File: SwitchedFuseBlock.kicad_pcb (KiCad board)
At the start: 2 copper layers, 9 parts

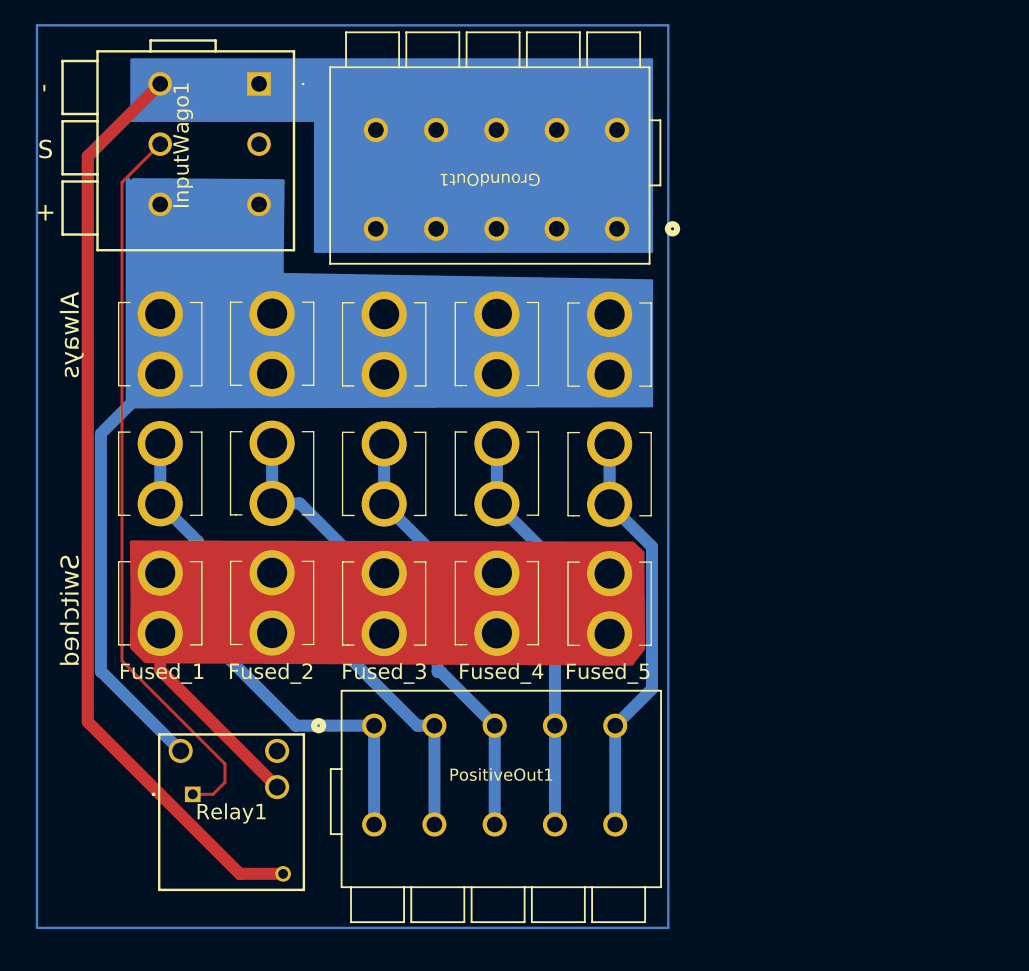
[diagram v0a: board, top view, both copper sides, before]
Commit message: Add flyback diode and thicker traces.
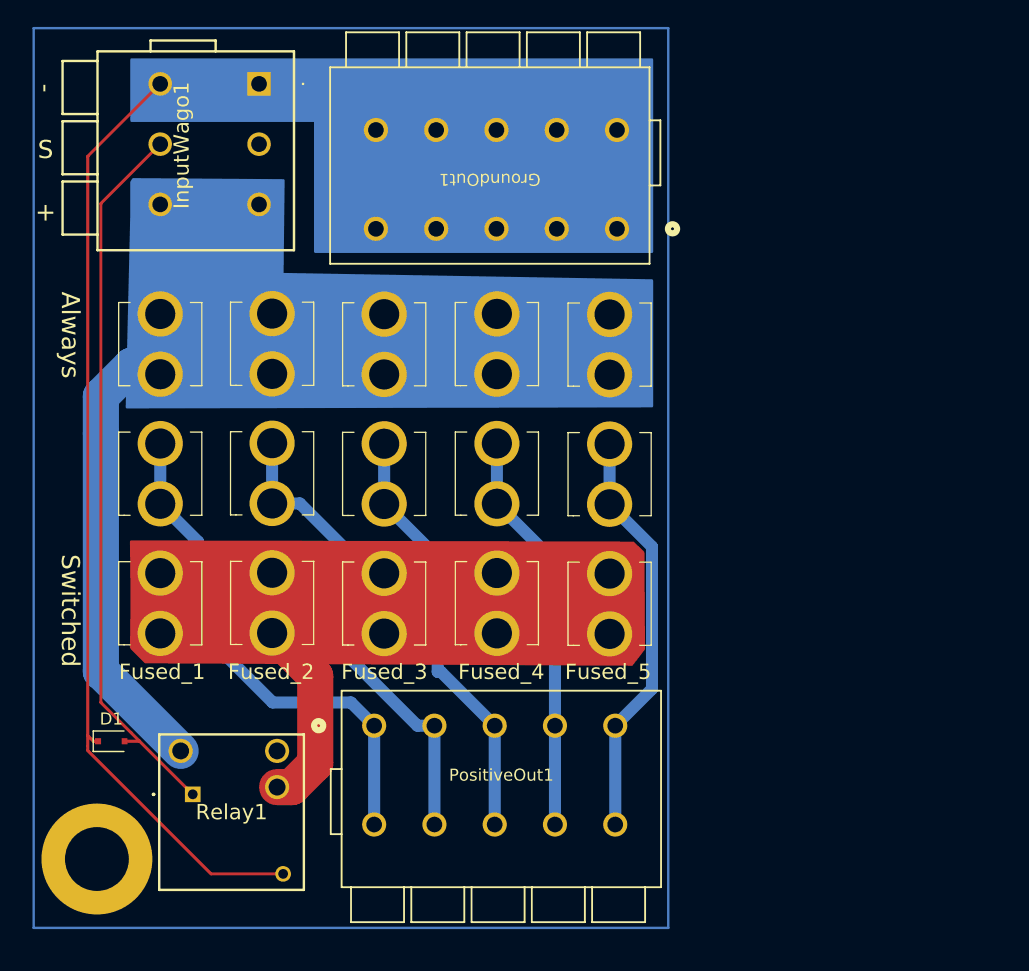
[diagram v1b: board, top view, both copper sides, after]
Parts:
- added D1: 1SS355VM, Diode_SMD:D_SOD-323F, F.Cu at (191.4, 99.7)
- added mounting_hole: MountingHole_5.3mm_M5_DIN965_Pad, MountingHole:MountingHole_5.3mm_M5_DIN965_Pad, F.Cu at (190.2, 109.5)
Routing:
- net Net-(Fused_1-Pad5): track 157.7 -> 160.5 mm
- net Net-(GroundOut1-Pad1): track 144.5 -> 147.0 mm
- net Net-(Relay1-Pad1): track 60.9 -> 60.4 mm

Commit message: Use mini fuse holders
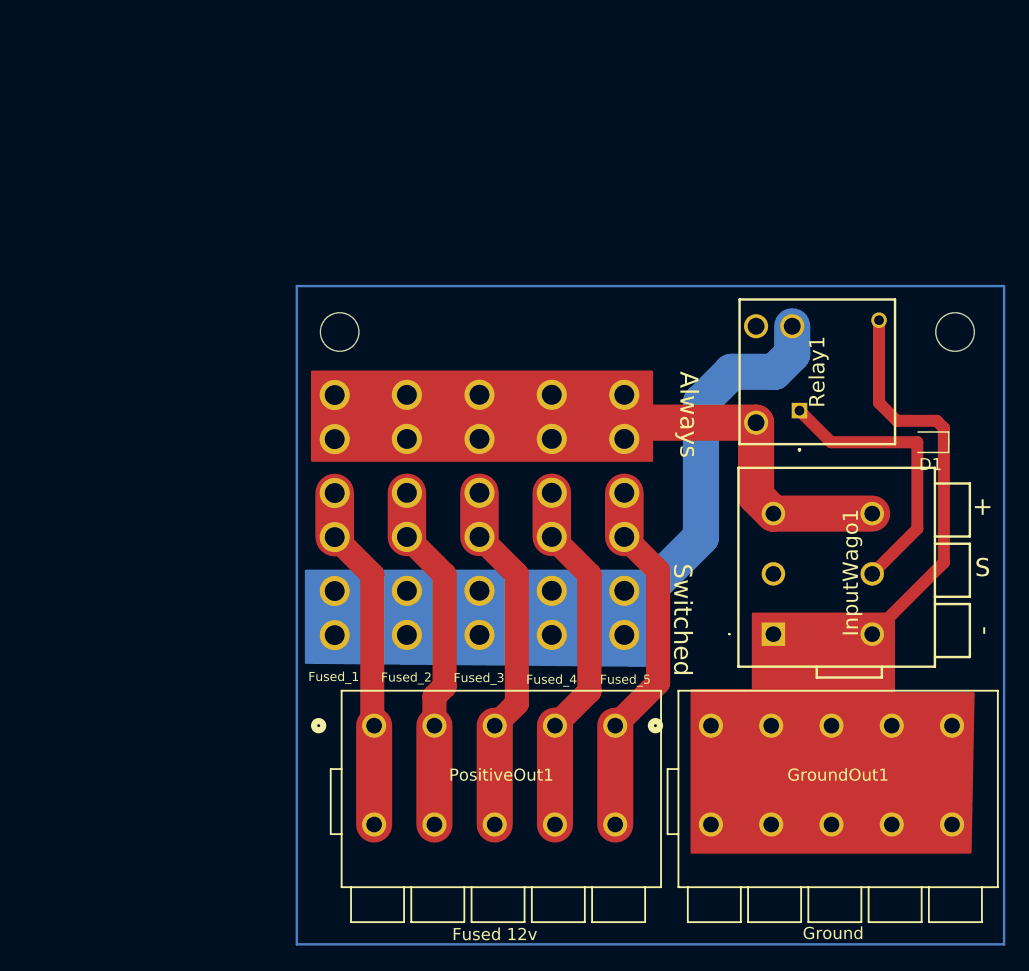
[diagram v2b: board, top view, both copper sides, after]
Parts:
- removed mounting_hole: MountingHole_5.3mm_M5_DIN965_Pad, MountingHole:MountingHole_5.3mm_M5_DIN965_Pad
- added Mounting Hole 1: MountingHole_3.2mm_M3, MountingHole:MountingHole_3.2mm_M3, F.Cu at (261.4, 65.8)
- added Mounting Hole 2: MountingHole_3.2mm_M3, MountingHole:MountingHole_3.2mm_M3, F.Cu at (210.3, 65.8)
- Fused_1, Fused_2, Fused_3, Fused_4, Fused_5: footprint LIB_01000057Z:2 Way Fuse -> LIB_01000057Z:2 Way Fuse (Mini)
- moved D1 72.4 mm to (259.3, 74.9), turned to 180 degrees
- moved InputWago1 62.5 mm to (246.3, 90.9), turned to 90 degrees
- moved Relay1 59.6 mm to (248.5, 72.3), turned to -90 degrees
- moved GroundOut1 42.0 mm to (241.1, 98.4), turned to 0 degrees
- moved Fused_1 14.5 mm to (209.9, 90.9)
- moved Fused_2 11.2 mm to (215.9, 90.9)
- moved Fused_3 7.91 mm to (221.9, 90.9)
- moved Fused_4 4.56 mm to (227.9, 90.9)
- moved Fused_5 1.22 mm to (233.9, 90.9)
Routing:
- net Net-(Fused_1-Pad5): track 160.5 -> 66.5 mm
- net Net-(D1-Pad1): track 147.0 -> 96.8 mm
- net Net-(Fused_1-Pad1): track 116.0 -> 73.3 mm
- net Net-(D1-Pad2): track 60.4 -> 23.3 mm
- net Net-(Fused_1-Pad3): track 42.9 -> 29.3 mm
- net Net-(Fused_2-Pad3): track 39.4 -> 29.2 mm
- net Net-(Fused_3-Pad3): track 35.9 -> 29.6 mm
- net Net-(Fused_5-Pad3): track 34.3 -> 30.2 mm
- net Net-(Fused_4-Pad3): track 33.6 -> 30.0 mm
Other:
- board text added: "Fused 12v"
- board text added: "Ground"
